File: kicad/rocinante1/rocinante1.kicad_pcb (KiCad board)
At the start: 2 copper layers, 7 parts, among them J1 Micro_SD_Card, U1 STM32H745IGTx

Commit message: checkpoint PCB work; schematic getting pretty close
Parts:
- added BT1: 1225, Battery:BatteryHolder_Keystone_3001_1x12mm, F.Cu at (166.0, 77.0)
- added C10: 100nF, Capacitor_SMD:C_0603_1608Metric, F.Cu at (130.4, 146.8)
- added C11: 100nF, Capacitor_SMD:C_0603_1608Metric, F.Cu at (125.4, 146.8)
- added C12: 100nF, Capacitor_SMD:C_0603_1608Metric, F.Cu at (114.8, 78.0)
- added C13: 100nF, Capacitor_SMD:C_0603_1608Metric, F.Cu at (125.4, 142.8)
- added C14: 100nF, Capacitor_SMD:C_0603_1608Metric, F.Cu at (125.4, 138.8)
- added C15: 100nF, Capacitor_SMD:C_0603_1608Metric, F.Cu at (125.4, 134.8)
- added C16: 100nF, Capacitor_SMD:C_0603_1608Metric, F.Cu at (114.8, 82.0)
- added C17: 100nF, Capacitor_SMD:C_0603_1608Metric, F.Cu at (198.0, 88.0)
- added C18: 70nF, Capacitor_SMD:C_0603_1608Metric, F.Cu at (228.4, 127.8)
- added C19: 70nF, Capacitor_SMD:C_0603_1608Metric, F.Cu at (232.5, 127.8)
- added C2: 100nF, Capacitor_SMD:C_0603_1608Metric, F.Cu at (138.0, 123.0)
- added C20: 1nF, Capacitor_SMD:C_0603_1608Metric, F.Cu at (111.8, 85.8)
- added C21: 100nF, Capacitor_SMD:C_0603_1608Metric, F.Cu at (211.0, 121.0)
- added C22: 100nF, Capacitor_SMD:C_0603_1608Metric, F.Cu at (203.0, 88.0)
- added C23: 100nF, Capacitor_SMD:C_0603_1608Metric, F.Cu at (116.5, 87.8)
- added C24: 100nF, Capacitor_SMD:C_0603_1608Metric, F.Cu at (124.2, 92.7)
- added C25: 10µF, Capacitor_SMD:C_0603_1608Metric, F.Cu at (198.0, 92.0)
- added C26: 10µF, Capacitor_SMD:C_0603_1608Metric, F.Cu at (206.0, 121.0)
- added C27: 10µF, Capacitor_SMD:C_0603_1608Metric, F.Cu at (173.0, 121.0)
- added C28: 100nF, Capacitor_SMD:C_0603_1608Metric, F.Cu at (201.0, 121.0)
- added C29: TBD, Capacitor_SMD:C_0603_1608Metric, F.Cu at (130.0, 99.0)
- added C3: 2.2µF, Capacitor_SMD:C_0603_1608Metric, F.Cu at (140.0, 98.0)
- added C30: TBD, Capacitor_SMD:C_0603_1608Metric, F.Cu at (106.5, 104.5)
- added C31: 100nF, Capacitor_SMD:C_0603_1608Metric, F.Cu at (125.4, 130.8)
- added C32: 100nF, Capacitor_SMD:C_0603_1608Metric, F.Cu at (228.4, 130.3)
- added C33: 1µF, Capacitor_SMD:C_0603_1608Metric, F.Cu at (228.4, 132.8)
- added C34: 4.7µF, Capacitor_SMD:C_0603_1608Metric, F.Cu at (191.0, 83.0)
- added C4: 100nF, Capacitor_SMD:C_0603_1608Metric, F.Cu at (120.4, 146.8)
- added C5: 2.2µF, Capacitor_SMD:C_0603_1608Metric, F.Cu at (211.0, 117.0)
- added C6: 100nF, Capacitor_SMD:C_0603_1608Metric, F.Cu at (198.0, 96.0)
- added C7: 100nF, Capacitor_SMD:C_0603_1608Metric, F.Cu at (120.4, 142.8)
- added C8: 100nF, Capacitor_SMD:C_0603_1608Metric, F.Cu at (125.4, 126.8)
- added C9: 100nF, Capacitor_SMD:C_0603_1608Metric, F.Cu at (130.4, 134.8)
- added D1: GREEN, LED_SMD:LED_0603_1608Metric, F.Cu at (129.2, 119.0)
- added D2: LED1, LED_SMD:LED_0603_1608Metric, F.Cu at (103.6, 112.5)
- added D3: LED2, LED_SMD:LED_0603_1608Metric, F.Cu at (99.5, 112.5)
- added D4: LED3, LED_SMD:LED_0603_1608Metric, F.Cu at (95.5, 112.5)
- added F1: F_Small, Fuse:Fuse_1210_3225Metric, F.Cu at (195.0, 122.0)
- added J10: KEYBOARD, Mini_din6:Mini_din6, F.Cu at (80.9, 97.3)
- added J11: SERIAL, Connector_PinHeader_2.54mm:PinHeader_1x06_P2.54mm_Vertical, F.Cu at (138.0, 105.0)
- added J12: SD_Card, Connector_Card:SD_Kyocera_145638009511859+, F.Cu at (102.2, 132.1)
- added J13: USBFS/POWER, Connector_USB:USB_Micro-B_Amphenol_10104110_Horizontal, F.Cu at (128.9, 63.4)
- added J14: I2S, Connector_PinHeader_2.54mm:PinHeader_1x06_P2.54mm_Vertical, F.Cu at (96.2, 91.5)
- added J15: EXPHDR, Connector_PinSocket_2.54mm:PinSocket_2x04_P2.54mm_Vertical, F.Cu at (168.1, 129.2)
- added J2: SWD, Connector_PinHeader_2.54mm:PinHeader_2x05_P2.54mm_Vertical, F.Cu at (147.0, 93.0)
- added J3: COMPOSITE, CUI_RCJ-044:CUI_RCJ-044, F.Cu at (115.0, 66.0)
- added J4: CTRL1, Connector_Dsub:DSUB-9_Male_Horizontal_P2.77x2.84mm_EdgePinOffset7.70mm_Housed_MountingHolesOffset9.12mm, F.Cu at (147.1, 138.9)
- added J5: CTRL2, Connector_Dsub:DSUB-9_Male_Horizontal_P2.77x2.84mm_EdgePinOffset7.70mm_Housed_MountingHolesOffset9.12mm, F.Cu at (180.3, 138.9)
- added J6: VGA, Connector_Dsub:DSUB-15-HD_Female_Horizontal_P2.29x1.98mm_EdgePinOffset3.03mm_Housed_MountingHolesOffset4.94mm, F.Cu at (184.3, 67.8)
- added J7: AudioIn, Connector_Audio:Jack_3.5mm_CUI_SJ1-3535NG_Horizontal, F.Cu at (102.1, 65.9)
- added J8: AudioOut, Connector_Audio:Jack_3.5mm_CUI_SJ1-3535NG_Horizontal, F.Cu at (90.2, 65.9)
- added J9: MOUSE, Mini_din6:Mini_din6, F.Cu at (209.1, 101.7)
- added R10: TBP, Resistor_SMD:R_0603_1608Metric, F.Cu at (149.0, 72.0)
- added R11: TBP, Resistor_SMD:R_0603_1608Metric, F.Cu at (154.0, 73.0)
- added R12: TBP, Resistor_SMD:R_0603_1608Metric, F.Cu at (148.0, 76.0)
- added R13: 47, Resistor_SMD:R_0603_1608Metric, F.Cu at (232.5, 130.3)
- added R14: 10K, Resistor_SMD:R_0603_1608Metric, F.Cu at (236.5, 127.8)
- added R15: 10K, Resistor_SMD:R_0603_1608Metric, F.Cu at (228.4, 135.3)
- added R16: 10K, Resistor_SMD:R_0603_1608Metric, F.Cu at (232.5, 132.8)
- added R21: 10K, Resistor_SMD:R_0603_1608Metric, F.Cu at (120.4, 130.8)
- added R22: 20K, Resistor_SMD:R_0603_1608Metric, F.Cu at (120.4, 126.8)
- added R23: 20K, Resistor_SMD:R_0603_1608Metric, F.Cu at (135.0, 95.0)
- added R24: 270, Resistor_SMD:R_0603_1608Metric, F.Cu at (154.0, 65.0)
- added R25: 560, Resistor_SMD:R_0603_1608Metric, F.Cu at (208.0, 85.0)
- added R26: 1100, Resistor_SMD:R_0603_1608Metric, F.Cu at (154.0, 77.0)
- added R27: 2.1k, Resistor_SMD:R_0603_1608Metric, F.Cu at (160.0, 62.0)
- added R28: 4.2k, Resistor_SMD:R_0603_1608Metric, F.Cu at (159.0, 66.0)
- added R29: 270, Resistor_SMD:R_0603_1608Metric, F.Cu at (211.0, 125.0)
- added R30: 560, Resistor_SMD:R_0603_1608Metric, F.Cu at (130.0, 91.0)
- added R31: 1100, Resistor_SMD:R_0603_1608Metric, F.Cu at (201.0, 125.0)
- added R32: 2.1k, Resistor_SMD:R_0603_1608Metric, F.Cu at (157.0, 118.0)
- added R33: 4.2k, Resistor_SMD:R_0603_1608Metric, F.Cu at (149.0, 114.0)
- added R34: 4.2k, Resistor_SMD:R_0603_1608Metric, F.Cu at (206.0, 125.0)
- added R35: 270, Resistor_SMD:R_0603_1608Metric, F.Cu at (135.0, 83.0)
- added R36: 560, Resistor_SMD:R_0603_1608Metric, F.Cu at (140.0, 86.0)
- added R37: 1100, Resistor_SMD:R_0603_1608Metric, F.Cu at (140.0, 94.0)
- added R38: 2.1k, Resistor_SMD:R_0603_1608Metric, F.Cu at (140.0, 90.0)
- added R39: 4.2k, Resistor_SMD:R_0603_1608Metric, F.Cu at (164.0, 87.0)
- added R40: 150, Resistor_SMD:R_0603_1608Metric, F.Cu at (198.0, 81.0)
- added R41: 150, Resistor_SMD:R_0603_1608Metric, F.Cu at (203.0, 81.0)
- added R42: 150, Resistor_SMD:R_0603_1608Metric, F.Cu at (208.0, 81.0)
- added R43: 20K, Resistor_SMD:R_0603_1608Metric, F.Cu at (91.7, 85.3)
- added R44: 20K, Resistor_SMD:R_0603_1608Metric, F.Cu at (96.7, 85.3)
- added R45: 20K, Resistor_SMD:R_0603_1608Metric, F.Cu at (135.0, 91.0)
- added R46: 20K, Resistor_SMD:R_0603_1608Metric, F.Cu at (135.0, 87.0)
- added R47: 20K, Resistor_SMD:R_0603_1608Metric, F.Cu at (84.0, 86.0)
- added R48: 20K, Resistor_SMD:R_0603_1608Metric, F.Cu at (125.0, 105.0)
- added R49: 68K, Resistor_SMD:R_0603_1608Metric, F.Cu at (164.0, 66.0)
- added R5: TBP, Resistor_SMD:R_0603_1608Metric, F.Cu at (135.0, 79.0)
- added R50: 68K, Resistor_SMD:R_0603_1608Metric, F.Cu at (169.0, 65.0)
- added R51: 68K, Resistor_SMD:R_0603_1608Metric, F.Cu at (143.1, 65.0)
- added R52: 68K, Resistor_SMD:R_0603_1608Metric, F.Cu at (147.8, 64.1)
- added R53: 68K, Resistor_SMD:R_0603_1608Metric, F.Cu at (98.5, 106.5)
- added R54: 68K, Resistor_SMD:R_0603_1608Metric, F.Cu at (104.5, 108.5)
- added R55: 22, Resistor_SMD:R_0603_1608Metric, F.Cu at (101.5, 102.5)
- added R56: 22, Resistor_SMD:R_0603_1608Metric, F.Cu at (120.9, 111.7)
- added R57: 22, Resistor_SMD:R_0603_1608Metric, F.Cu at (92.5, 101.5)
- added R58: 22, Resistor_SMD:R_0603_1608Metric, F.Cu at (119.0, 105.0)
- added R59: 22, Resistor_SMD:R_0603_1608Metric, F.Cu at (93.5, 105.5)
- added R6: TBP, Resistor_SMD:R_0603_1608Metric, F.Cu at (151.0, 81.0)
- added R60: 22, Resistor_SMD:R_0603_1608Metric, F.Cu at (109.3, 98.2)
- added R61: TBD, Resistor_SMD:R_0603_1608Metric, F.Cu at (135.0, 99.0)
- added R62: TBD, Resistor_SMD:R_0603_1608Metric, F.Cu at (149.0, 108.0)
- added R63: 10K, Resistor_SMD:R_0603_1608Metric, F.Cu at (80.0, 107.0)
- added R64: 10K, Resistor_SMD:R_0603_1608Metric, F.Cu at (208.0, 90.0)
- added R65: 10K, Resistor_SMD:R_0603_1608Metric, F.Cu at (79.0, 86.0)
- added R66: 10K, Resistor_SMD:R_0603_1608Metric, F.Cu at (211.0, 110.0)
- added R7: TBP, Resistor_SMD:R_0603_1608Metric, F.Cu at (154.0, 69.0)
- added R8: TBP, Resistor_SMD:R_0603_1608Metric, F.Cu at (140.0, 79.0)
- added R9: TBP, Resistor_SMD:R_0603_1608Metric, F.Cu at (146.0, 80.0)
- added SW1: RESET, Button_Switch_SMD:SW_Push_1P1T_NO_6x6mm_H9.5mm, F.Cu at (141.7, 73.0)
- added SW2: USER1, Button_Switch_SMD:SW_Push_1P1T_NO_6x6mm_H9.5mm, F.Cu at (182.2, 120.3)
- added SW3: USER2, Button_Switch_SMD:SW_Push_1P1T_NO_6x6mm_H9.5mm, F.Cu at (125.7, 82.8)
- added SW4: USER3, Button_Switch_SMD:SW_Push_1P1T_NO_6x6mm_H9.5mm, F.Cu at (146.3, 120.7)
- added SW5: BOOT0, Button_Switch_SMD:SW_Push_1P1T_NO_6x6mm_H9.5mm, F.Cu at (165.0, 119.8)
- added U2: W9812G6KH-5, Package_SO:TSOP-II-54_22.2x10.16mm_P0.8mm, F.Cu at (159.0, 103.0)
- added U3: LD1117S33TR_SOT223, Package_TO_SOT_SMD:SOT-223-3_TabPin2, F.Cu at (201.1, 112.3)
- added X1: ASE-14.31818MHz, Oscillator:Oscillator_SMD_Abracon_ASE-4Pin_3.2x2.5mm, F.Cu at (198.0, 104.0)
- added Y1: 25MHz, Crystal:Crystal_SMD_2016-4Pin_2.0x1.6mm, F.Cu at (212.0, 90.0)
- C1: value 10µF -> 100nF; footprint Capacitor_SMD:CP_Elec_8x6.2 -> Capacitor_SMD:C_0603_1608Metric
- J1: value Micro_SD_Card -> ESP_01; footprint Connector_Card:microSD_HC_Molex_104031-0811 -> Connector_PinSocket_2.54mm:PinSocket_2x04_P2.54mm_Vertical
- R1, R2, R3, R4: value 68K -> 220; footprint Resistor_SMD:R_0805_2012Metric_Pad1.15x1.40mm_HandSolder -> Resistor_SMD:R_0603_1608Metric
- U1: value STM32H745IGTx -> STM32H743IITx
- moved U1 59.8 mm to (181.0, 100.0)
- moved R4 51.3 mm to (120.0, 101.0), turned to 0 degrees
- moved R1 47.9 mm to (130.0, 123.0), turned to 0 degrees
- moved R3 44.5 mm to (125.0, 101.0), turned to 0 degrees
- moved R2 37.6 mm to (130.0, 95.0), turned to 0 degrees
- moved C1 29.9 mm to (130.4, 138.8)
- moved J1 28.1 mm to (154.0, 87.0)
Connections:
- net Net-(U1-Pad41) renamed USART2_RTS
- C1 pad 1: VDD3.3 -> +3V3
- J1 pad 1: Net-(J1-Pad1) -> GND
- J1 pad 2: SPIO_CS -> ESP_TX
- J1 pad 3: SPIO_DI -> ESP_GPIO2
- J1 pad 4: VDD3.3 -> ESP_CH_EN
- J1 pad 5: SPIO_SCK -> ESP_GPIO0
- J1 pad 6: GND -> ESP_RST
- J1 pad 7: SPIO_DO -> ESP_RX
- J1 pad 8: Net-(J1-Pad8) -> +3V3
- R1 pad 1: VDD3.3 -> +3V3
- R1 pad 2: SPIO_DO -> Net-(D1-Pad2)
- R2 pad 1: Net-(R2-Pad1) -> LED1
- R2 pad 2: SPIO_SCK -> Net-(D2-Pad2)
- R3 pad 1: Net-(R3-Pad1) -> LED2
- R3 pad 2: SPIO_DI -> Net-(D3-Pad2)
- R4 pad 1: VDD3.3 -> LED3
- R4 pad 2: SPIO_CS -> Net-(D4-Pad2)
- U1 pad 1: Net-(U1-Pad1) -> USER1
- U1 pad 10: Net-(U1-Pad10) -> VGA_R4
- U1 pad 100: Net-(U1-Pad100) -> TIM4_CH1
- U1 pad 102: Net-(U1-Pad102) -> GND
- U1 pad 103: Net-(U1-Pad103) -> +3V3
- U1 pad 104: Net-(U1-Pad104) -> SDRAM_D0
- U1 pad 105: Net-(U1-Pad105) -> SDRAM_D1
- U1 pad 106: Net-(U1-Pad106) -> SDIO_CD
- U1 pad 107: Net-(U1-Pad107) -> SPI6_NSS_SWCTL
- U1 pad 108: Net-(U1-Pad108) -> SDRAM_BA0
- U1 pad 109: Net-(U1-Pad109) -> SDRAM_BA1
- U1 pad 11: Net-(U1-Pad11) -> ESP_TX
- U1 pad 110: Net-(U1-Pad110) -> ESP_RST
- U1 pad 111: Net-(U1-Pad111) -> ESP_CH_EN
- U1 pad 112: Net-(U1-Pad112) -> SDRAM_SDCLK
- U1 pad 113: Net-(U1-Pad113) -> GND
- U1 pad 114: Net-(U1-Pad114) -> +3V3
- U1 pad 115: Net-(U1-Pad115) -> VGA_G1
- U1 pad 116: Net-(U1-Pad116) -> VGA_G2
- U1 pad 117: Net-(U1-Pad117) -> VGA_G3
- U1 pad 118: Net-(U1-Pad118) -> VGA_G4
- U1 pad 119: Net-(U1-Pad119) -> TIM2_CH1
- U1 pad 12: Net-(U1-Pad12) -> FIRE1
- U1 pad 120: Net-(U1-Pad120) -> TIM1_CH2
- U1 pad 121: Net-(U1-Pad121) -> USART1_RX
- U1 pad 122: Net-(U1-Pad122) -> USB_FS_D_N
- U1 pad 123: Net-(U1-Pad123) -> USB_FS_D_P
- U1 pad 124: Net-(U1-Pad124) -> SWDIO
- U1 pad 126: Net-(U1-Pad126) -> GND
- U1 pad 127: Net-(U1-Pad127) -> +3V3
- U1 pad 128: Net-(U1-Pad128) -> S2
- U1 pad 129: Net-(U1-Pad129) -> W2
- U1 pad 13: Net-(U1-Pad13) -> FIRE2
- U1 pad 130: Net-(U1-Pad130) -> E2
- U1 pad 131: Net-(U1-Pad131) -> CV0
- U1 pad 132: Net-(U1-Pad132) -> CV1
- U1 pad 133: Net-(U1-Pad133) -> CV2
- U1 pad 134: Net-(U1-Pad134) -> CV3
- U1 pad 135: Net-(U1-Pad135) -> GND
- U1 pad 136: Net-(U1-Pad136) -> +3V3
- U1 pad 137: Net-(U1-Pad137) -> SWCLK
- U1 pad 138: Net-(U1-Pad138) -> TIM2_CH1
- U1 pad 139: Net-(U1-Pad139) -> VGA_G5
- U1 pad 14: Net-(U1-Pad14) -> GND
- U1 pad 140: Net-(U1-Pad140) -> VGA_R0
- U1 pad 141: Net-(U1-Pad141) -> VGA_R1
- U1 pad 142: Net-(U1-Pad142) -> SDRAM_D2
- U1 pad 143: Net-(U1-Pad143) -> SDRAM_D3
- U1 pad 144: Net-(U1-Pad144) -> EXP01
- U1 pad 145: Net-(U1-Pad145) -> EXP02
- U1 pad 148: Net-(U1-Pad148) -> GND
- U1 pad 149: Net-(U1-Pad149) -> +3V3
- U1 pad 15: Net-(U1-Pad15) -> +3V3
- U1 pad 150: Net-(U1-Pad150) -> SDIO_CLK
- U1 pad 151: Net-(U1-Pad151) -> SDIO_CMD
- U1 pad 152: Net-(U1-Pad152) -> I2S_SDI
- U1 pad 153: Net-(U1-Pad153) -> I2S_WS
- U1 pad 154: Net-(U1-Pad154) -> I2S_CK
- U1 pad 155: Net-(U1-Pad155) -> SPI6_MISO
- U1 pad 156: Net-(U1-Pad156) -> SPI6_SCK
- U1 pad 157: Net-(U1-Pad157) -> SPI6_MOSI
- U1 pad 158: Net-(U1-Pad158) -> GND
- U1 pad 159: Net-(U1-Pad159) -> +3V3
- U1 pad 16: Net-(U1-Pad16) -> SDRAM_A0
- U1 pad 160: Net-(U1-Pad160) -> SDRAM_SDNCAS
- U1 pad 161: Net-(U1-Pad161) -> SDIO_D2
- U1 pad 162: Net-(U1-Pad162) -> SDIO_D3
- U1 pad 163: Net-(U1-Pad163) -> TIM3_CH2
- U1 pad 164: Net-(U1-Pad164) -> USART1_RX
- U1 pad 165: Net-(U1-Pad165) -> I2C1_SDA
- U1 pad 166: Net-(U1-Pad166) -> BOOT
- U1 pad 167: Net-(U1-Pad167) -> I2C1_SCL
- U1 pad 168: Net-(U1-Pad168) -> ESP_RX
- U1 pad 169: Net-(U1-Pad169) -> SDRAM_NBL0
- U1 pad 17: Net-(U1-Pad17) -> SDRAM_A1
- U1 pad 170: Net-(U1-Pad170) -> SDRAM_NBL1
- U1 pad 171: Net-(U1-Pad171) -> +3V3
- U1 pad 172: Net-(U1-Pad172) -> +3V3
- U1 pad 173: GND -> CV4
- U1 pad 174: Net-(U1-Pad174) -> CV5
- U1 pad 175: Net-(U1-Pad175) -> CV6
- U1 pad 176: VDD3.3 -> CV7
- U1 pad 18: Net-(U1-Pad18) -> SDRAM_A2
- U1 pad 19: Net-(U1-Pad19) -> SDRAM_A3
- U1 pad 2: Net-(U1-Pad2) -> USER2
- U1 pad 20: Net-(U1-Pad20) -> SDRAM_A4
- U1 pad 21: Net-(U1-Pad21) -> SDRAM_A5
- U1 pad 22: Net-(U1-Pad22) -> GND
- U1 pad 23: Net-(U1-Pad23) -> +3V3
- U1 pad 24: Net-(U1-Pad24) -> LED2
- U1 pad 25: Net-(U1-Pad25) -> ADC3_INP3
- U1 pad 26: Net-(U1-Pad26) -> ADC3_INP7
- U1 pad 27: Net-(U1-Pad27) -> ADC3_INP2
- U1 pad 28: Net-(U1-Pad28) -> ADC3_INP6
- U1 pad 29: Net-(U1-Pad29) -> CLOCK0
- U1 pad 3: Net-(U1-Pad3) -> USER3
- U1 pad 30: Net-(U1-Pad30) -> CLOCK1
- U1 pad 31: Net-(U1-Pad31) -> NRST
- U1 pad 32: Net-(U1-Pad32) -> VGA_B0
- U1 pad 33: Net-(U1-Pad33) -> VGA_B1
- U1 pad 34: Net-(U1-Pad34) -> VGA_B2
- U1 pad 35: Net-(U1-Pad35) -> VGA_B3
- U1 pad 36: Net-(U1-Pad36) -> +3V3
- U1 pad 37: Net-(U1-Pad37) -> GND
- U1 pad 38: Net-(U1-Pad38) -> VREFP
- U1 pad 39: Net-(U1-Pad39) -> +3V3
- U1 pad 4: Net-(U1-Pad4) -> LED1
- U1 pad 40: Net-(U1-Pad40) -> USART2_CTS
- U1 pad 42: Net-(U1-Pad42) -> USART2_TX
- U1 pad 43: Net-(U1-Pad43) -> SDRAM_SDCKE0
- U1 pad 44: Net-(U1-Pad44) -> SDRAM_SDNE0
- U1 pad 46: Net-(U1-Pad46) -> SDRAM_SDNWE
- U1 pad 47: Net-(U1-Pad47) -> USART2_RX
- U1 pad 48: Net-(U1-Pad48) -> GND
- U1 pad 49: Net-(U1-Pad49) -> +3V3
- U1 pad 5: Net-(U1-Pad5) -> LED3
- U1 pad 50: Net-(U1-Pad50) -> DAC1_OUT1
- U1 pad 51: Net-(U1-Pad51) -> DAC1_OUT2
- U1 pad 52: Net-(U1-Pad52) -> ADC1_INP3
- U1 pad 53: Net-(U1-Pad53) -> I2S1_SDO
- U1 pad 54: Net-(U1-Pad54) -> VGA_B4
- U1 pad 55: Net-(U1-Pad55) -> VGA_G0
- U1 pad 57: Net-(U1-Pad57) -> ADC1_INP5
- U1 pad 59: Net-(U1-Pad59) -> SDRAM_SDNRAS
- U1 pad 6: GND -> BAT
- U1 pad 60: Net-(U1-Pad60) -> SDRAM_A6
- U1 pad 61: Net-(U1-Pad61) -> GND
- U1 pad 62: Net-(U1-Pad62) -> +3V3
- U1 pad 63: Net-(U1-Pad63) -> SDRAM_A7
- U1 pad 64: Net-(U1-Pad64) -> SDRAM_A8
- U1 pad 65: Net-(U1-Pad65) -> SDRAM_A9
- U1 pad 66: Net-(U1-Pad66) -> SDRAM_A10
- U1 pad 67: Net-(U1-Pad67) -> SDRAM_A11
- U1 pad 68: Net-(U1-Pad68) -> SDRAM_D4
- U1 pad 69: Net-(U1-Pad69) -> SDRAM_D5
- U1 pad 7: VDD3.3 -> Net-(U1-Pad7)
- U1 pad 70: Net-(U1-Pad70) -> SDRAM_D6
- U1 pad 71: Net-(U1-Pad71) -> GND
- U1 pad 72: Net-(U1-Pad72) -> +3V3
- U1 pad 73: Net-(U1-Pad73) -> SDRAM_D7
- U1 pad 74: Net-(U1-Pad74) -> SDRAM_D8
- U1 pad 75: Net-(U1-Pad75) -> SDRAM_D9
- U1 pad 76: Net-(U1-Pad76) -> SDRAM_D10
- U1 pad 77: Net-(U1-Pad77) -> SDRAM_D11
- U1 pad 78: Net-(U1-Pad78) -> SDRAM_D12
- U1 pad 79: Net-(U1-Pad79) -> USART3_RX
- U1 pad 8: Net-(U1-Pad8) -> VGA_R2
- U1 pad 80: Net-(U1-Pad80) -> USART3_RX
- U1 pad 82: Net-(U1-Pad82) -> +3V3
- U1 pad 83: Net-(U1-Pad83) -> N1
- U1 pad 84: Net-(U1-Pad84) -> S1
- U1 pad 85: Net-(U1-Pad85) -> W1
- U1 pad 86: Net-(U1-Pad86) -> E1
- U1 pad 88: Net-(U1-Pad88) -> TIM5_CH2
- U1 pad 89: Net-(U1-Pad89) -> N2
- U1 pad 9: Net-(U1-Pad9) -> VGA_R3
- U1 pad 90: Net-(U1-Pad90) -> GND
- U1 pad 91: Net-(U1-Pad91) -> +3V3
- U1 pad 92: Net-(U1-Pad92) -> TIM3_CH2
- U1 pad 94: Net-(U1-Pad94) -> SDIO_D0
- U1 pad 95: Net-(U1-Pad95) -> SDIO_D1
- U1 pad 96: Net-(U1-Pad96) -> SDRAM_D13
- U1 pad 97: Net-(U1-Pad97) -> SDRAM_D14
- U1 pad 98: Net-(U1-Pad98) -> SDRAM_D15
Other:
- board outline added: 138.6 x 89.2 mm
- board text added: "1225 COIN CELL"
- board text added: "AUDIO_IN"
- board text added: "AUDIO_OUT"
- board text added: "CTRL1"
- board text added: "CTRL2"
- board text added: "POWER USB DEVICE"
- board text added: "VGA"

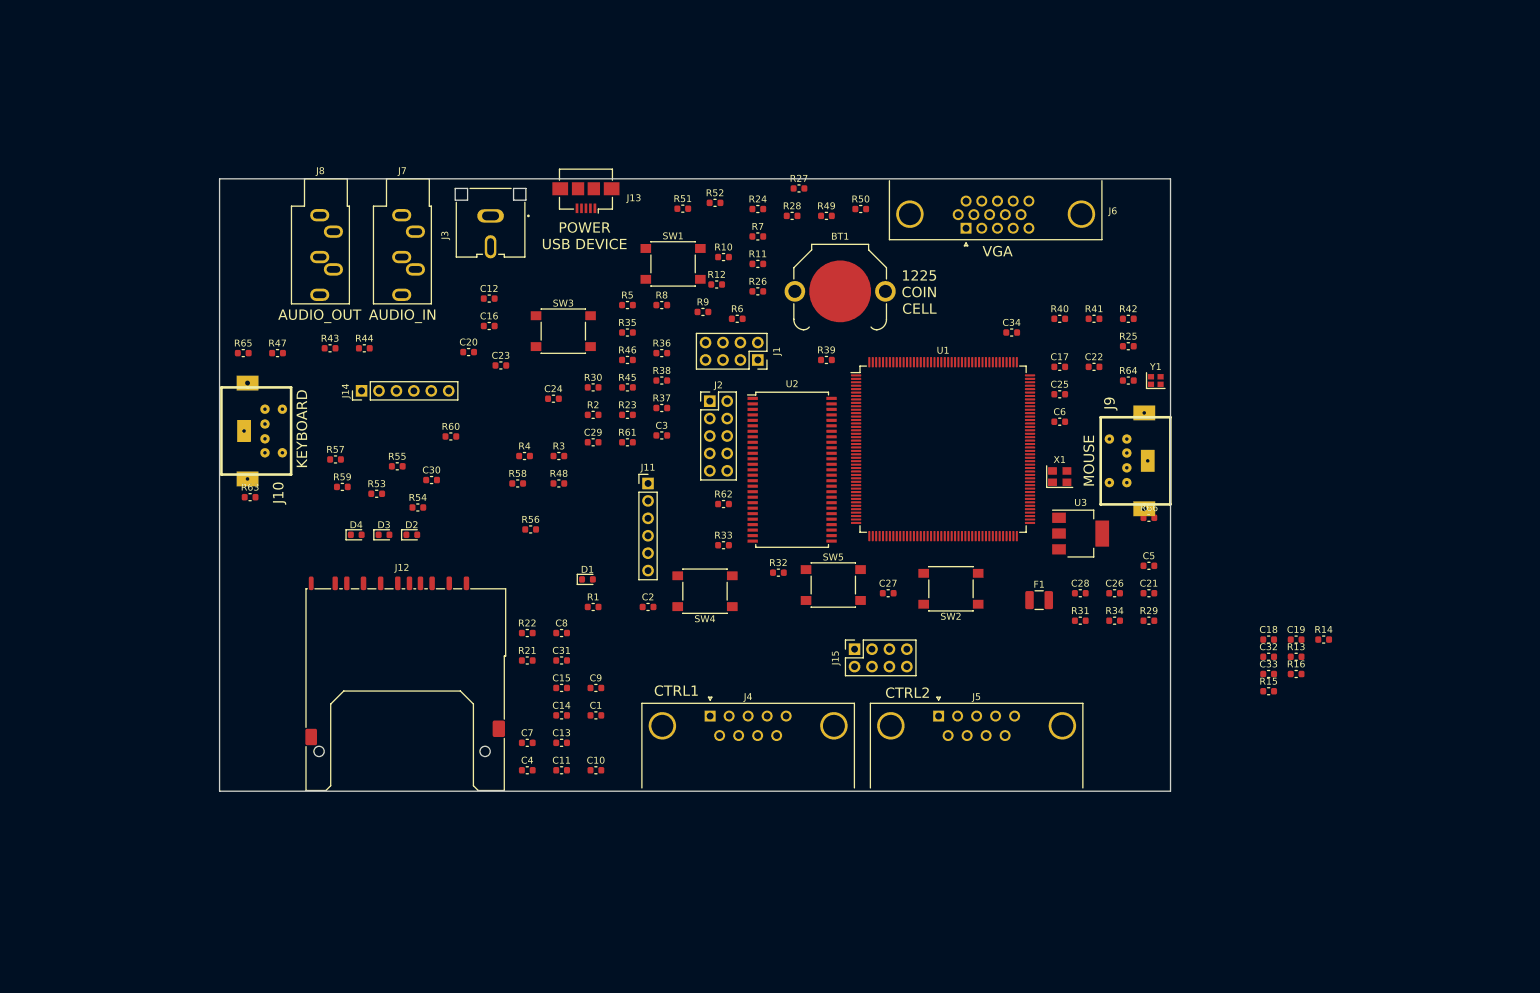
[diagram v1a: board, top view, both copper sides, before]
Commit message: finish schematic draft; place some parts
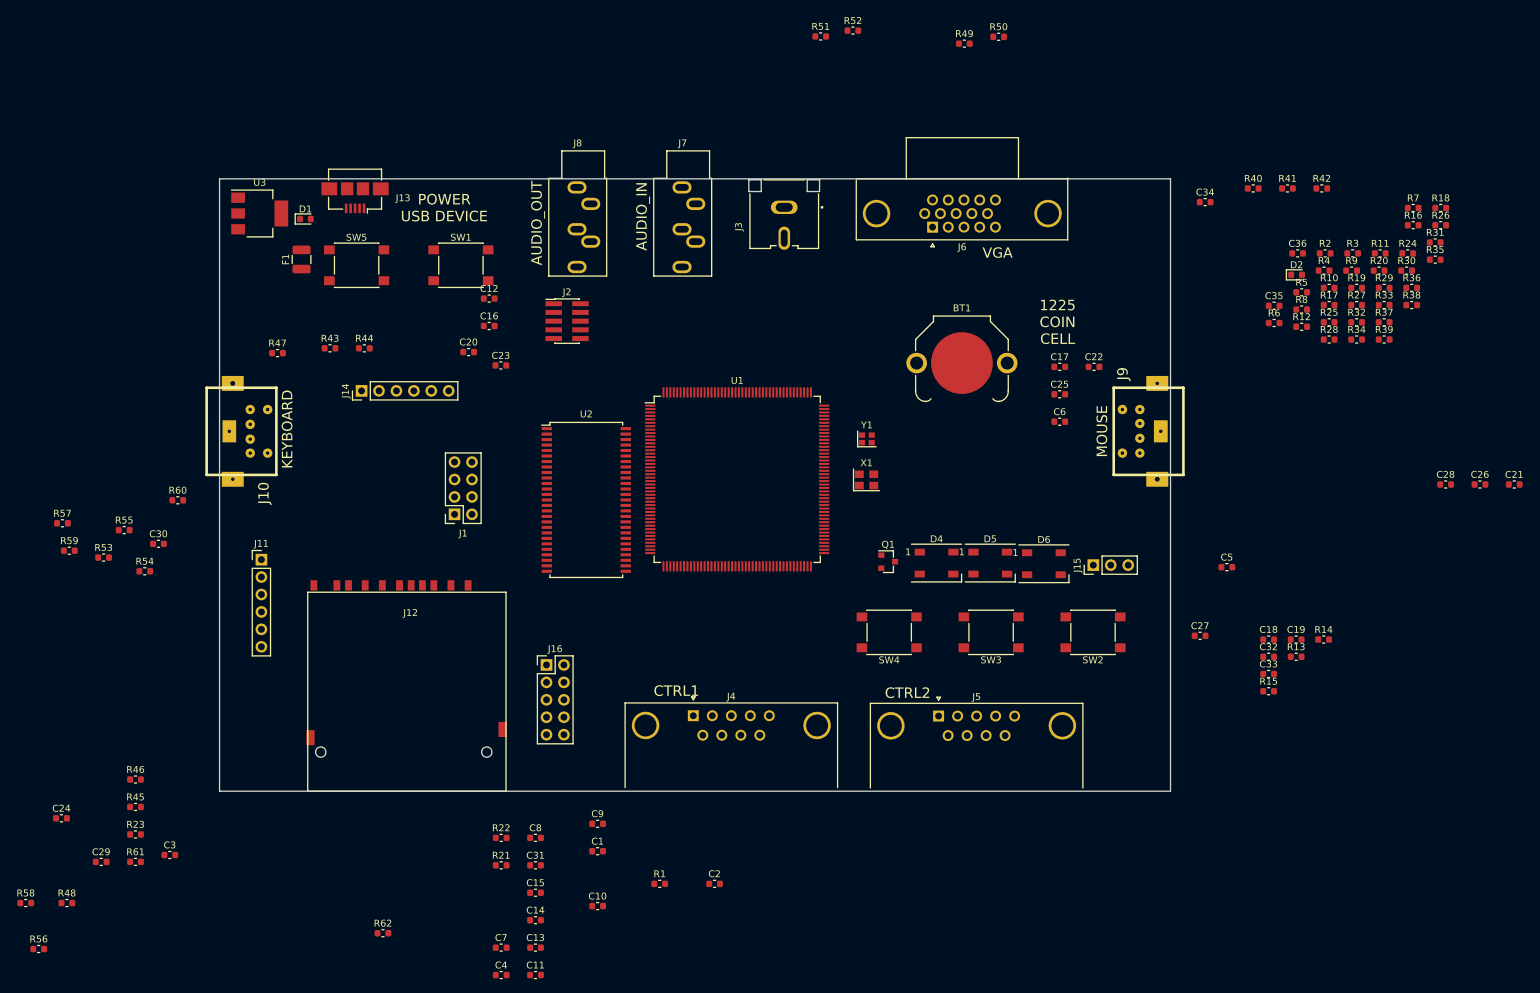
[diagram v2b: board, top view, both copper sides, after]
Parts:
- removed D3: LED2, LED_SMD:LED_0603_1608Metric
- removed R63, R64, R65, R66: 10K, Resistor_SMD:R_0603_1608Metric
- added C35: 1µF, Capacitor_SMD:C_0603_1608Metric, F.Cu at (229.2, 79.1)
- added C36: 1µF, Capacitor_SMD:C_0603_1608Metric, F.Cu at (232.7, 71.5)
- added D5: RGBLED2, LED_SMD:LED_WS2812B_PLCC4_5.0x5.0mm_P3.2mm, F.Cu at (187.9, 116.6)
- added D6: RGBLED3, LED_SMD:LED_WS2812B_PLCC4_5.0x5.0mm_P3.2mm, F.Cu at (195.7, 116.7)
- added J16: EXPHDR, Connector_PinHeader_2.54mm:PinHeader_2x05_P2.54mm_Vertical, F.Cu at (123.2, 131.4)
- added Q1: Q_NPN_CBE, Package_TO_SOT_SMD:SOT-23, F.Cu at (173.0, 116.4)
- added R17: 270, Resistor_SMD:R_0603_1608Metric, F.Cu at (237.3, 79.0)
- added R18: 560, Resistor_SMD:R_0603_1608Metric, F.Cu at (253.5, 64.8)
- added R19: 1100, Resistor_SMD:R_0603_1608Metric, F.Cu at (241.3, 76.5)
- added R20: 2.2k, Resistor_SMD:R_0603_1608Metric, F.Cu at (244.6, 74.0)
- D1: value GREEN -> POWERLED
- D2: value LED1 -> DEBUGLED
- D4: value LED3 -> RGBLED1; footprint LED_SMD:LED_0603_1608Metric -> LED_SMD:LED_WS2812B_PLCC4_5.0x5.0mm_P3.2mm
- J12: footprint Connector_Card:SD_Kyocera_145638009511859+ -> Connector_FCI:10067847-001RLF
- J15: value EXPHDR -> NEOPIXEL; footprint Connector_PinSocket_2.54mm:PinSocket_2x04_P2.54mm_Vertical -> Connector_PinHeader_2.54mm:PinHeader_1x03_P2.54mm_Vertical
- J2: footprint Connector_PinHeader_2.54mm:PinHeader_2x05_P2.54mm_Vertical -> Connector_PinHeader_1.27mm:PinHeader_2x05_P1.27mm_Vertical_SMD
- J6: footprint Connector_Dsub:DSUB-15-HD_Female_Horizontal_P2.29x1.98mm_EdgePinOffset3.03mm_Housed_MountingHolesOffset4.94mm -> DSUB15HD:HD15-SN-24
- J7: value AudioIn -> AUDIOIN
- J8: value AudioOut -> AUDIOOUT
- R10: value TBP -> 6.9k
- R11: value TBP -> 14k
- R12: value TBP -> 28K
- R2: value 220 -> 2.2k
- R24, R29, R35: value 270 -> 4.3k
- R25: value 560 -> 270
- R26: value 1100 -> 560
- R27: value 2.1k -> 1100
- R28, R34: value 4.2k -> 2.2k
- R3: value 220 -> 6.8k
- R30: value 560 -> 8.6k
- R31: value 1100 -> 270
- R32: value 2.1k -> 560
- R33: value 4.2k -> 1100
- R36: value 560 -> 10K
- R37: value 1100 -> 10K
- R38: value 2.1k -> 10K
- R39: value 4.2k -> 10K
- R5: value TBP -> 215
- R6: value TBP -> 430
- R7: value TBP -> 860
- R8: value TBP -> 1.7k
- R9: value TBP -> 3.4k
- U2: value W9812G6KH-5 -> W9812G6KH-6
- moved D2 134.4 mm to (232.5, 74.6)
- moved U3 128.4 mm to (81.4, 65.7)
- moved R30 119.8 mm to (248.6, 74.0)
- moved R4 119.6 mm to (236.5, 74.0)
- moved R3 119.4 mm to (240.7, 71.5)
- moved F1 118.4 mm to (87.5, 72.3), turned to 90 degrees
- moved R35 118.2 mm to (252.7, 72.4)
- moved R38 109.9 mm to (249.3, 79.0)
- moved R36 109.7 mm to (249.3, 76.5)
- moved R2 109.3 mm to (236.7, 71.5)
- moved R37 106.0 mm to (245.3, 81.5)
- moved R33 102.5 mm to (245.3, 79.0)
- moved R26 100.0 mm to (253.5, 67.4)
- moved R5 98.3 mm to (233.3, 77.1)
- moved R7 95.6 mm to (249.5, 64.8)
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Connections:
- C1 pad 1: +3V3 -> VDD
- C10 pad 1: +3V3 -> VDD
- C11 pad 1: +3V3 -> VDD
- C12 pad 1: +3V3 -> VDD
- C13 pad 1: +3V3 -> VDD
- C14 pad 1: +3V3 -> VDD
- C15 pad 1: +3V3 -> VDD
- C16 pad 1: +3V3 -> VDD
- C17 pad 1: +3V3 -> VDD
- C18 pad 1: +3V3 -> VDD
- C19 pad 1: +3V3 -> VDD
- C2 pad 1: +3V3 -> VDD
- C25 pad 1: +3V3 -> VDD
- C27 pad 1: +3V3 -> VDD
- C31 pad 1: +3V3 -> VDD
- C34 pad 1: +3V3 -> VDD
- C4 pad 1: +3V3 -> VDD
- C6 pad 1: +3V3 -> VDD
- C7 pad 1: +3V3 -> VDD
- C8 pad 1: +3V3 -> VDD
- C9 pad 1: +3V3 -> VDD
- D4 pad 1: GND -> +5V
- J1 pad 8: +3V3 -> VDD
- J12 pad 11: Net-(J12-Pad11) -> SDIO_WP
- J12 pad 4: +3V3 -> VDD
- J14 pad 1: +3V3 -> VDD
- J15 pad 1: SPI6_MISO -> +5V
- J15 pad 2: +3V3 -> Net-(D6-Pad2)
- J15 pad 3: SPI6_SCK -> GND
- J2 pad 1: +3V3 -> VDD
- J4 pad 7: +5V -> JOYSELECT
- J4 pad 8: GND -> KEYSELECT
- J5 pad 7: +5V -> JOYSELECT
- J5 pad 8: GND -> KEYSELECT
- R1 pad 1: +3V3 -> VDD
- R13 pad 1: +3V3 -> VDD
- R14 pad 1: +3V3 -> VDD
- R15 pad 1: +3V3 -> VDD
- R16 pad 1: +3V3 -> MOUSE_DATA
- R16 pad 2: Net-(R16-Pad2) -> +5V
- R2 pad 1: LED1 -> Net-(Q1-Pad2)
- R2 pad 2: Net-(D2-Pad2) -> VDD
- R25 pad 1: VGA_BLUE -> VGA_GREEN
- R25 pad 2: VGA_B1 -> VGA_G5
- R26 pad 1: VGA_BLUE -> VGA_GREEN
- R26 pad 2: VGA_B2 -> VGA_G4
- R27 pad 1: VGA_BLUE -> VGA_GREEN
- R27 pad 2: VGA_B3 -> VGA_G3
- R28 pad 1: VGA_BLUE -> VGA_GREEN
- R28 pad 2: VGA_B4 -> VGA_G2
- R29 pad 2: VGA_G0 -> VGA_G1
- R3 pad 1: LED2 -> Net-(D4-Pad4)
- R3 pad 2: Net-(D3-Pad2) -> +5V
- R30 pad 2: VGA_G1 -> VGA_G0
- R31 pad 1: VGA_GREEN -> VGA_RED
- R31 pad 2: VGA_G2 -> VGA_R4
- R32 pad 1: VGA_GREEN -> VGA_RED
- R32 pad 2: VGA_G3 -> VGA_R3
- R33 pad 1: VGA_GREEN -> VGA_RED
- R33 pad 2: VGA_G4 -> VGA_R2
- R34 pad 1: VGA_GREEN -> VGA_RED
- R34 pad 2: VGA_G5 -> VGA_R1
- R36 pad 1: VGA_RED -> KBD_DATA
- R36 pad 2: VGA_R1 -> +5V
- R37 pad 1: VGA_RED -> MOUSE_CLK
- R37 pad 2: VGA_R2 -> +5V
- R38 pad 1: VGA_RED -> KBD_CLK
- R38 pad 2: VGA_R3 -> +5V
- R39 pad 1: VGA_RED -> Net-(R39-Pad1)
- R39 pad 2: VGA_R4 -> VDD
- R4 pad 1: LED3 -> DEBUG
- R4 pad 2: Net-(D4-Pad2) -> Net-(D2-Pad2)
- R49 pad 2: +3V3 -> VDD
- R50 pad 2: +3V3 -> VDD
- R51 pad 2: +3V3 -> VDD
- R52 pad 2: +3V3 -> VDD
- R53 pad 2: +3V3 -> VDD
- R54 pad 2: +3V3 -> VDD
- SW2 pad 1: +3V3 -> VDD
- SW3 pad 1: +3V3 -> VDD
- SW4 pad 1: +3V3 -> VDD
- SW5 pad 1: +3V3 -> VDD
- U1 pad 101: Net-(U1-Pad101) -> RGBLED_PWM
- U1 pad 103: +3V3 -> VDD
- U1 pad 114: +3V3 -> VDD
- U1 pad 127: +3V3 -> VDD
- U1 pad 136: +3V3 -> VDD
- U1 pad 144: EXP01 -> EXPGPIO0
- U1 pad 145: EXP02 -> EXPGPIO1
- U1 pad 149: +3V3 -> VDD
- U1 pad 15: +3V3 -> VDD
- U1 pad 159: +3V3 -> VDD
- U1 pad 171: +3V3 -> VDD
- U1 pad 172: +3V3 -> VDD
- U1 pad 23: +3V3 -> VDD
- U1 pad 24: LED2 -> EXPPWM
- U1 pad 36: +3V3 -> VDD
- U1 pad 39: +3V3 -> VDD
- U1 pad 4: LED1 -> DEBUG
- U1 pad 49: +3V3 -> VDD
- U1 pad 5: LED3 -> RGBLED_PWM
- U1 pad 56: Net-(U1-Pad56) -> SDIO_WP
- U1 pad 58: Net-(U1-Pad58) -> JOYSELECT
- U1 pad 62: +3V3 -> VDD
- U1 pad 72: +3V3 -> VDD
- U1 pad 82: +3V3 -> VDD
- U1 pad 91: +3V3 -> VDD
- U1 pad 93: Net-(U1-Pad93) -> KEYSELECT
- U2 pad 1: +3V3 -> VDD
- U2 pad 14: +3V3 -> VDD
- U2 pad 27: +3V3 -> VDD
- U2 pad 3: +3V3 -> VDD
- U2 pad 43: +3V3 -> VDD
- U2 pad 49: +3V3 -> VDD
- U2 pad 9: +3V3 -> VDD
- U3 pad 2: +3V3 -> VDD
- X1 pad 1: Net-(R16-Pad2) -> Net-(R39-Pad1)
- X1 pad 4: +3V3 -> VDD
